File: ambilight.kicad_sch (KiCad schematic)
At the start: 31 parts, among them J1 TYPE-C-31-M-12, J2 RGB Connector, J3 Power Connector, SW1 RESET, SW2 BOOT, U1 AZ1117CR-3.3TRG1, U2 ESP32-C3-MINI-1-H4, U3 MCP1416, U4 USBLC6-2SC6

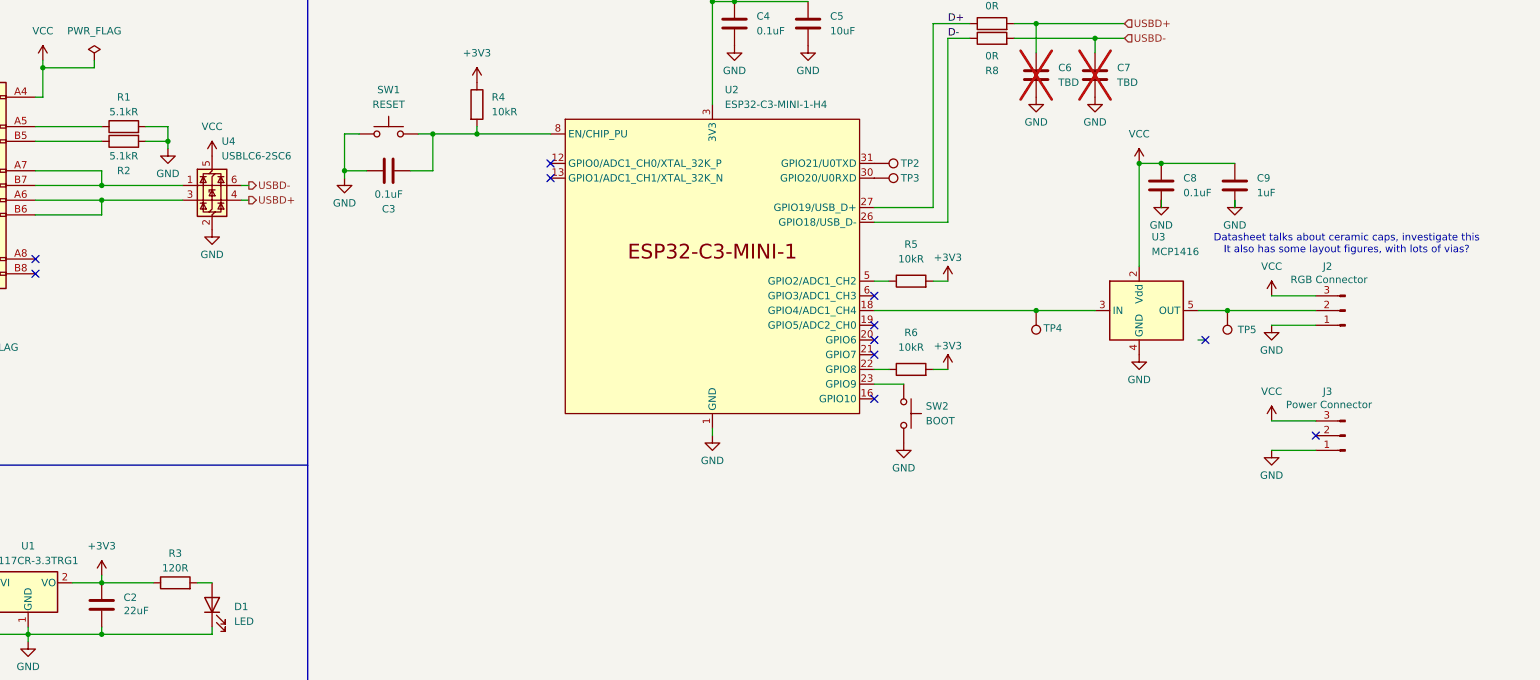
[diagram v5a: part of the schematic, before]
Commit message: Fix resistor values
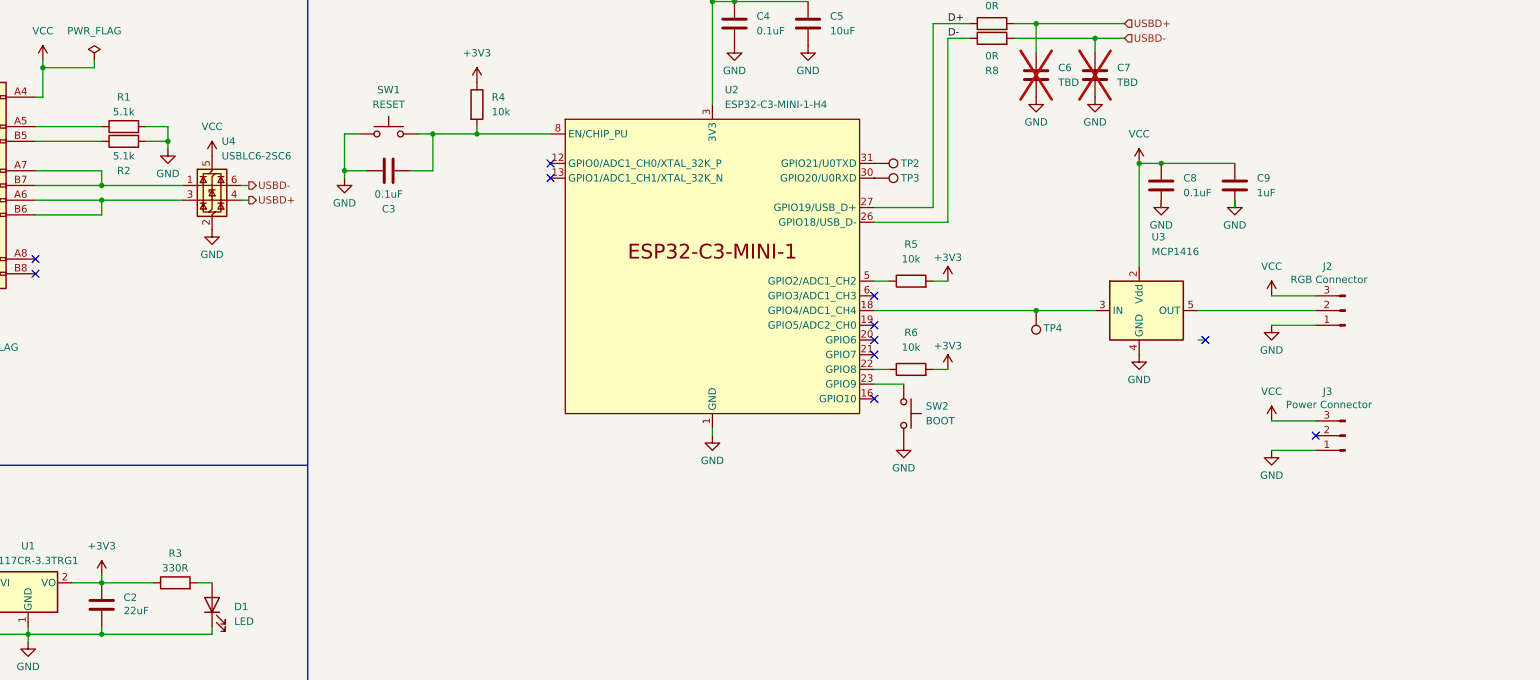
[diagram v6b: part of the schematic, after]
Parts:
- removed TP5: ~, Custom_PCBWay:TestPoint_Pad_D1.0mm_SilkscreenFix, symbol Connector:TestPoint
- R1, R2: value 5.1kR -> 5.1k
- R3: value 120R -> 330R
- R4, R5, R6: value 10kR -> 10k
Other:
- note removed: "Datasheet talks about ceramic caps, investigate this It also has some layout figures, with lots of vias?"
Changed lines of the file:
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@@
 	(generator_version "9.0")
 	(paper "A4")
-	(text "Datasheet talks about ceramic caps, investigate this\nIt also has some layout figures, with lots of vias?"
-		(exclude_from_sim no)
-		(at 268.224 68.58 0)
-		(effects
-			(font
-				(size 1.27 1.27)
-			)
-		)
-	)
 	(text "ESP32 + Level Shifter"
 		(exclude_from_sim no)
@@
 	)
 	(junction
-		(at 247.65 80.01)
-		(diameter 0)
-		(color 0 0 0 0)
-	)
-	(junction
 		(at 53.34 127)
 		(diameter 0)
@@
 		)
 	)
-	(wire
-		(pts
-			(xy 242.57 80.01) (xy 247.65 80.01)
-		)
-		(stroke
-			(width 0)
-			(type default)
-		)
-	)
 	(polyline
 		(pts
@@
 	(wire
 		(pts
-			(xy 247.65 80.01) (xy 262.89 80.01)
+			(xy 242.57 80.01) (xy 262.89 80.01)
 		)
 		(stroke
@@
 	)
 	(symbol
-		(lib_id "Connector:TestPoint")
-		(at 247.65 80.01 180)
-		(unit 1)
-		(exclude_from_sim no)
-		(in_bom yes)
-		(on_board yes)
-		(dnp no)
-		(property "Reference" "TP5"
-			(at 249.428 83.312 0)
-			(effects
-				(font
-					(size 1.27 1.27)
-				)
-				(justify right)
-			)
-		)
-		(property "Value" "~"
-			(at 250.19 84.582 0)
-			(effects
-				(font
-					(size 1.27 1.27)
-				)
-				(justify right)
-			)
-		)
-		(property "Footprint" "Custom_PCBWay:TestPoint_Pad_D1.0mm_SilkscreenFix"
-			(at 242.57 80.01 0)
-			(effects
-				(font
-					(size 1.27 1.27)
-				)
-				(hide yes)
-			)
-		)
-		(property "Datasheet" "~"
-			(at 242.57 80.01 0)
-			(effects
-				(font
-					(size 1.27 1.27)
-				)
-				(hide yes)
-			)
-		)
-		(property "Description" "test point"
-			(at 247.65 80.01 0)
-			(effects
-				(font
-					(size 1.27 1.27)
-				)
-				(hide yes)
-			)
-		)
-		(pin "1"
-		)
-		(instances
-			(project ""
-				(path "/3b2736b3-ab99-437a-a7b8-84251aa18a5c"
-					(reference "TP5")
-					(unit 1)
-				)
-			)
-		)
-	)
-	(symbol
 		(lib_id "power:GND")
 		(at 158.75 101.6 0)
@@
 			)
 		)
-		(property "Value" "10kR"
+		(property "Value" "10k"
 			(at 120.65 45.7199 0)
 			(effects
@@
 			)
 		)
-		(property "Value" "10kR"
+		(property "Value" "10k"
 			(at 193.04 86.36 90)
 			(effects
@@
 			)
 		)
-		(property "Value" "120R"
+		(property "Value" "330R"
 			(at 66.04 124.46 90)
 			(effects
@@
 			)
 		)
-		(property "Value" "5.1kR"
+		(property "Value" "5.1k"
 			(at 57.15 45.72 90)
 			(effects
@@
 			)
 		)
-		(property "Value" "10kR"
+		(property "Value" "10k"
 			(at 193.04 71.12 90)
 			(effects
@@
 			)
 		)
-		(property "Value" "5.1kR"
+		(property "Value" "5.1k"
 			(at 57.15 53.34 90)
 			(effects

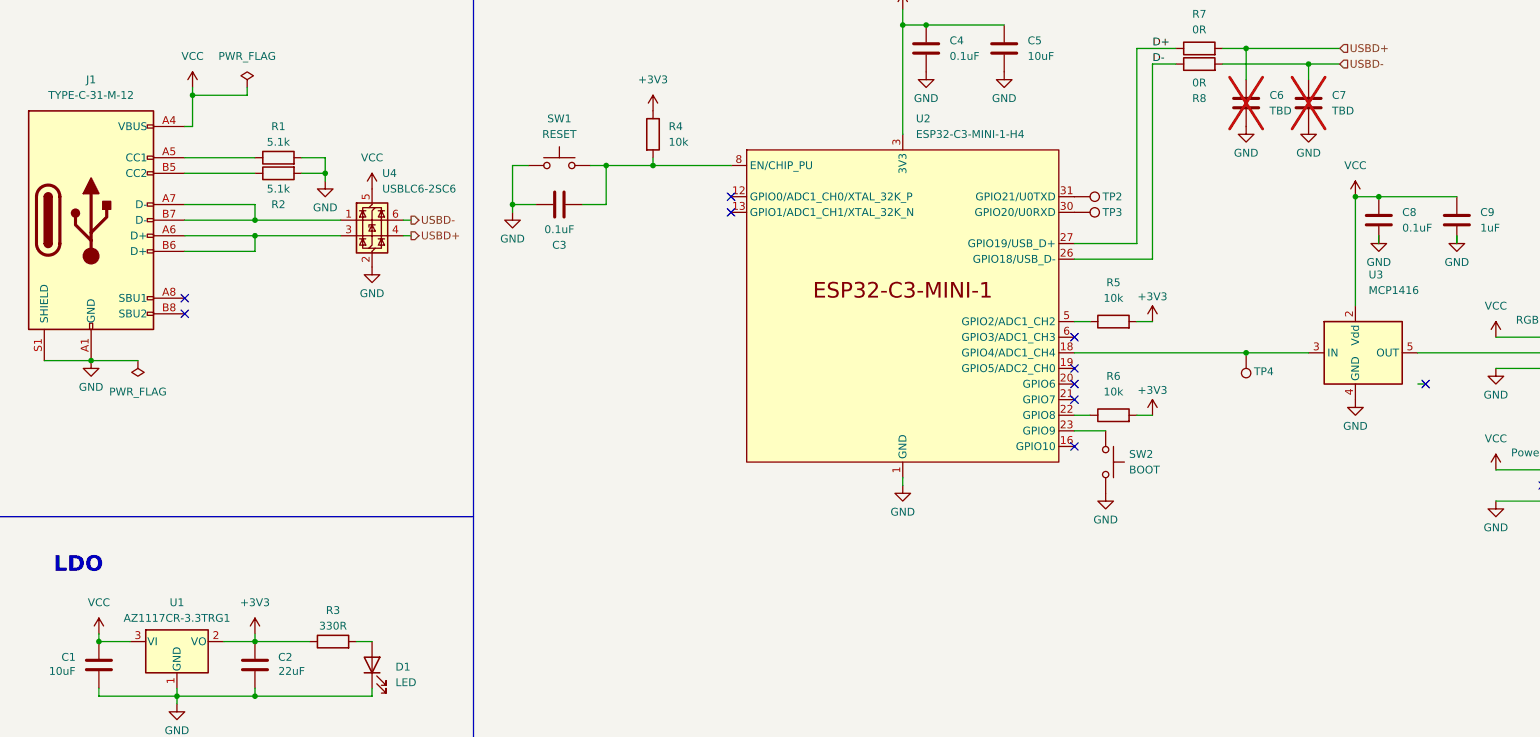
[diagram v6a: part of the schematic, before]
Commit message: Many small-ish changes, generate production files
Some components were changed to get better deal at manufacturer. The
files in the production folder are the ones sent to the manufacturer for
this release.
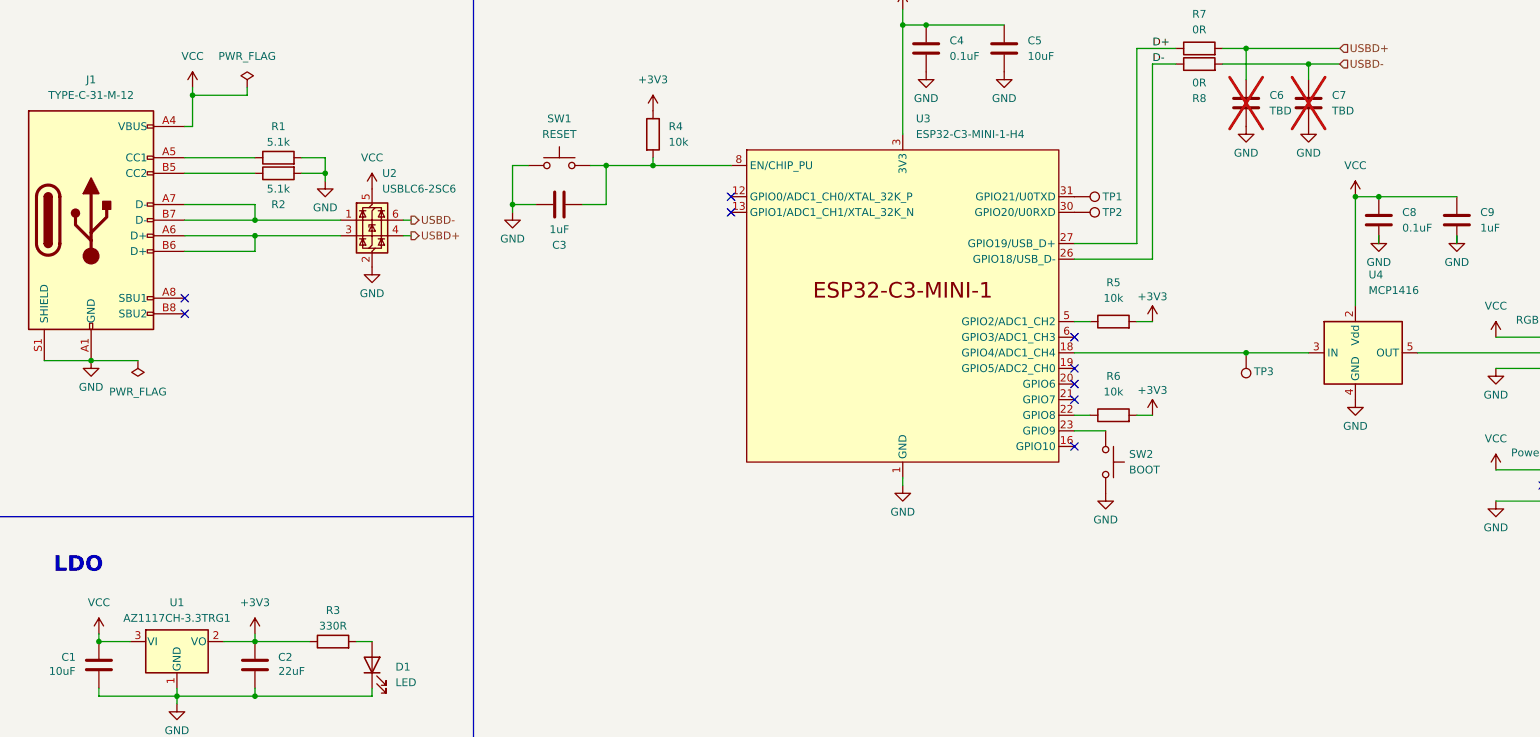
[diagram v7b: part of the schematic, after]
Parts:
- C3: value 0.1uF -> 1uF
- J1: PosOffset (none) -> 0,1.4605
- J2, J3: JLCPCB Part # (none) -> C49257; RotOffset (none) -> 90
- SW1, SW2: footprint Button_Switch_SMD:SW_Push_1P1T_NO_CK_KMR2 -> Button_Switch_additional:TS-1088-AR02016; JLCPCB Part # (none) -> C720477; RotOffset (none) -> 90
- TP1: renamed from TP2; now left out of the parts list
- TP2: renamed from TP3; now left out of the parts list
- TP3: renamed from TP4; now left out of the parts list
- U1: value AZ1117CR-3.3TRG1 -> AZ1117CH-3.3TRG1; footprint Package_TO_SOT_SMD:SOT-89-3_Handsoldering -> Package_TO_SOT_SMD:SOT-223-3_TabPin2
- U2: renamed from U4; RotOffset (none) -> 90
- U3: renamed from U2; JLCPCB Part # (none) -> C41349510; PosOffset (none) -> 0,-2.7305
- U4: renamed from U3; RotOffset (none) -> 90
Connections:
- net GND: now also SW1.2; no longer SW1.1
- net at C3.1, R4.2, U3.8 (EN/CHIP_PU): now also SW1.1; no longer SW1.2
- no-connect marks 11 -> 10
